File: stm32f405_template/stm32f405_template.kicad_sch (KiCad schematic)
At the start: 55 parts, among them J1 USB_B, J2 Conn_01x08, J3 Conn_01x08, J4 Conn_01x02, J5 Conn_01x08, J6 Conn_01x08, J7 Conn_01x02, J8 Conn_01x02, Q1 2N3904, Q2 2N3904, SW1 SW_RESET, U1 STM32F405RGTx, U2 MCP1700-3302E_TO92, Y1 14MHz, Y2 32.768 kHz

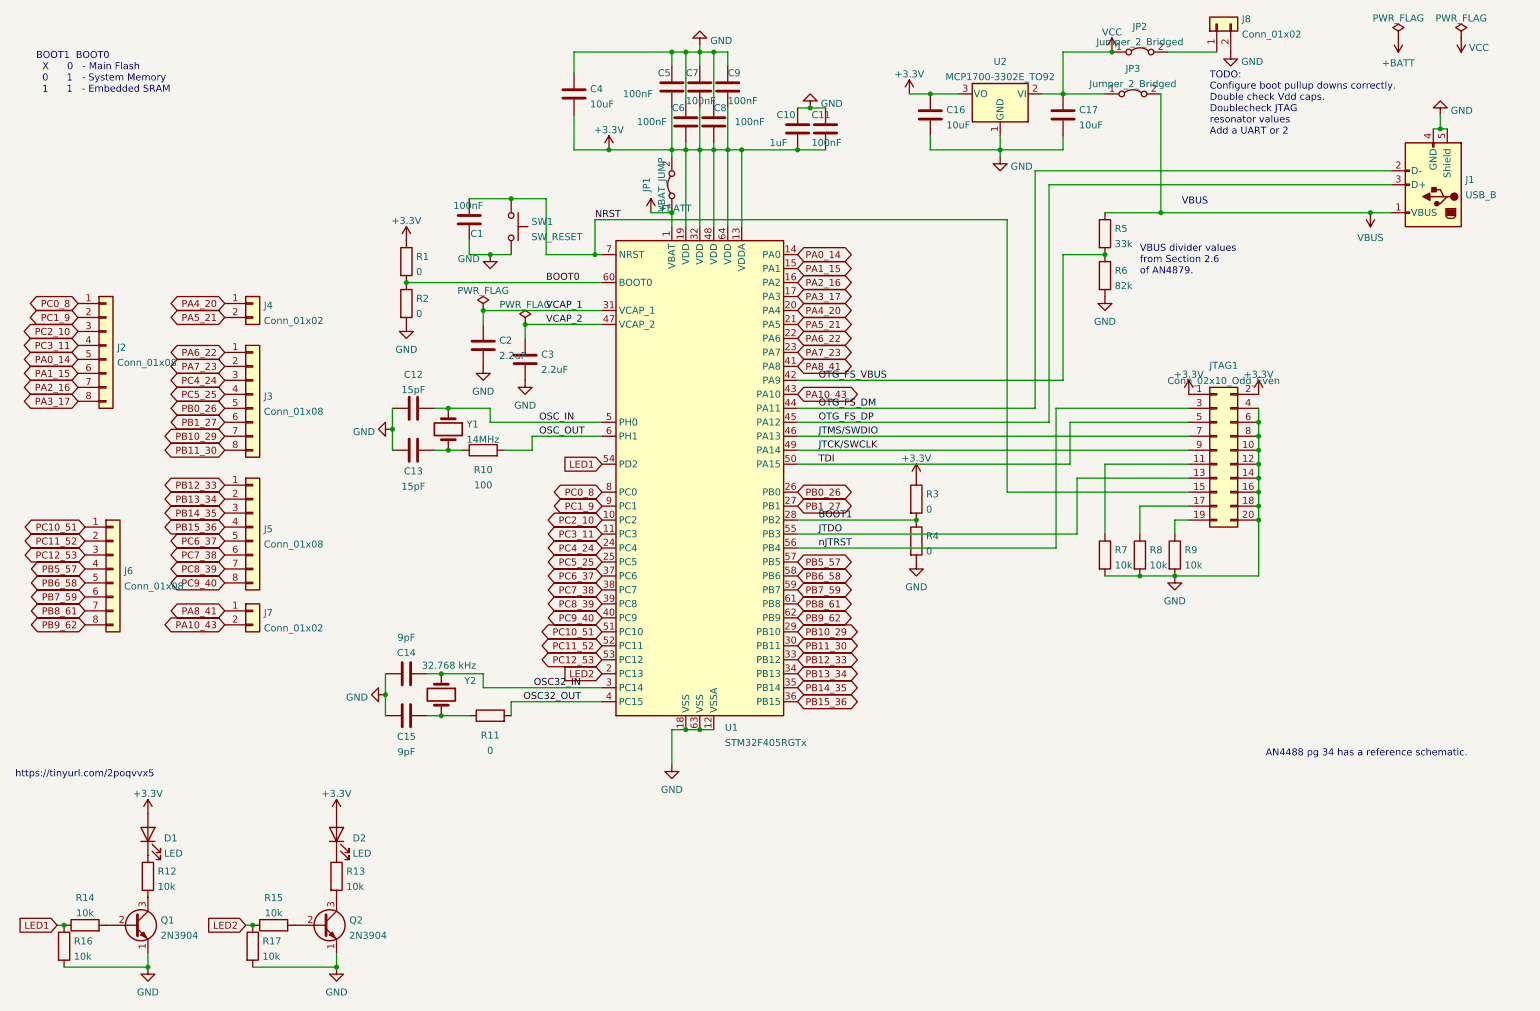
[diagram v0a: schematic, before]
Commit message: Geographic re-annotate and cleanup
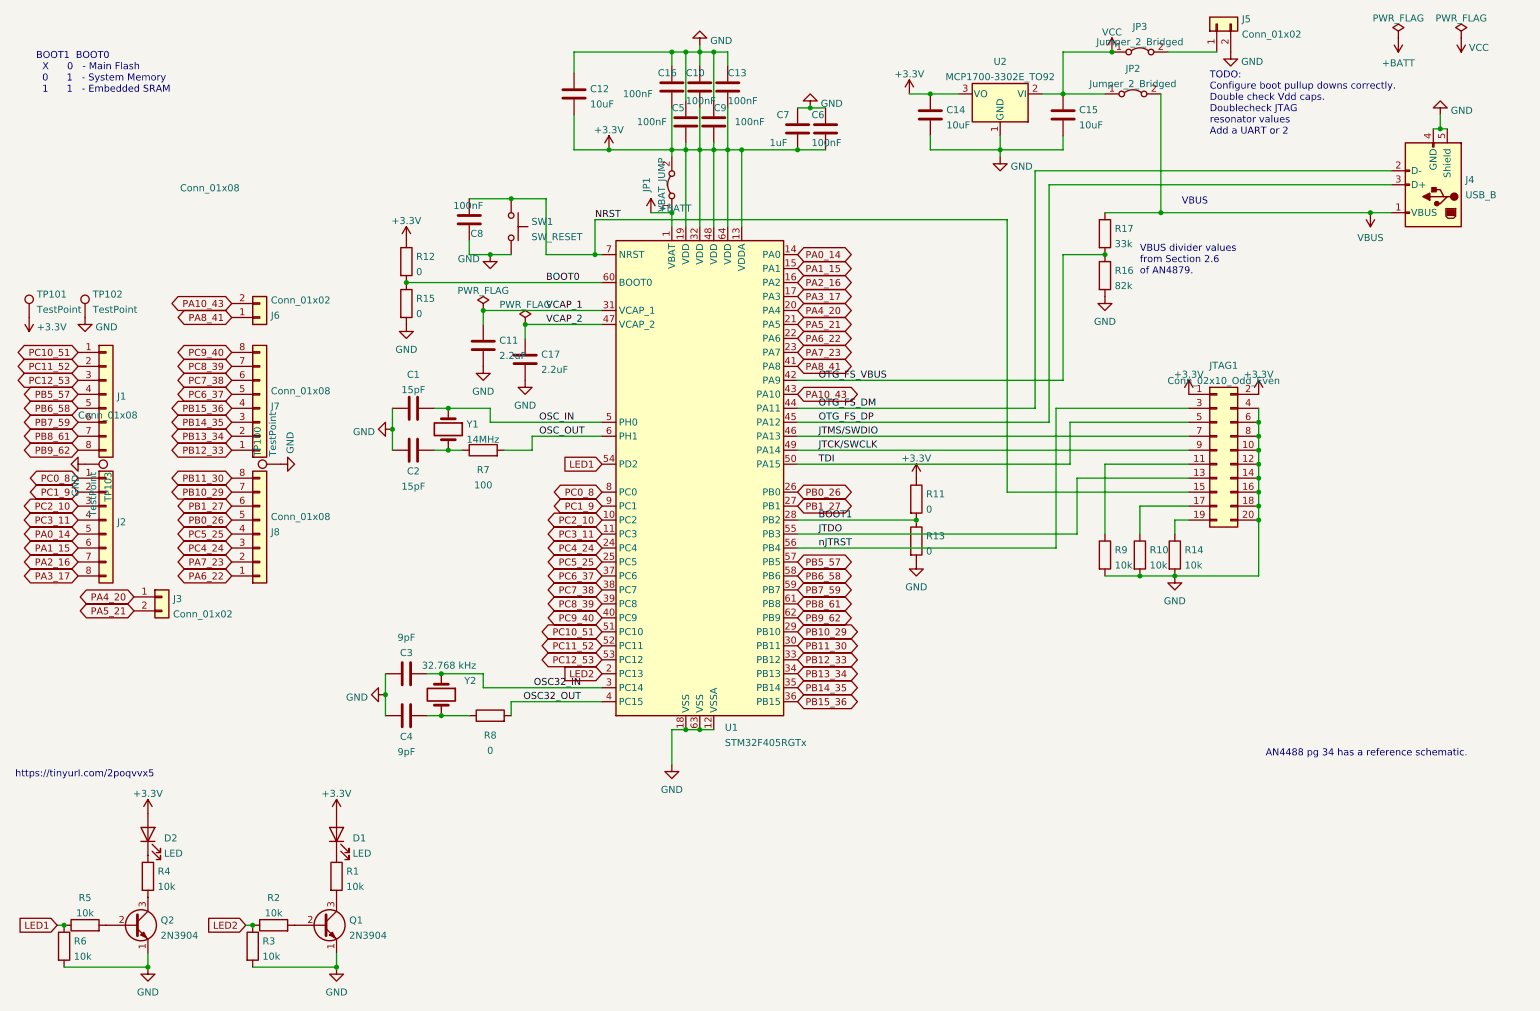
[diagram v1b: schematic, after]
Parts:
- added TP100, TP102, TP103: TestPoint, TestPoint:TestPoint_THTPad_1.5x1.5mm_Drill0.7mm, symbol Connector:TestPoint
- added TP101: TestPoint, TestPoint:TestPoint_THTPad_D1.5mm_Drill0.7mm, symbol Connector:TestPoint
- renumbered C12 to C1, C7 to C10, C2 to C11, C4 to C12, C9 to C13, C16 to C14, C17 to C15, C5 to C16, C3 to C17, C13 to C2, C14 to C3, C15 to C4, C6 to C5, C11 to C6, C10 to C7, C1 to C8, C8 to C9, D2 to D1, D1 to D2, J6 to J1, J4 to J3, J1 to J4, J8 to J5, J7 to J6, J5 to J7, J3 to J8, JP3 to JP2, JP2 to JP3, Q2 to Q1, Q1 to Q2, R13 to R1, R8 to R10, R3 to R11, R1 to R12, R4 to R13, R9 to R14, R2 to R15, R6 to R16, R5 to R17, R15 to R2, R17 to R3, R12 to R4, R14 to R5, R16 to R6, R10 to R7, R11 to R8, R7 to R9
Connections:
- net +3.3V: now also TP101.1
- net GND: now also TP100.1, TP102.1, TP103.1
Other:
- moved on the sheet: J1, J2, J3, J6, J7, J8

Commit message: Tidied silkscreen and some routing cleanup
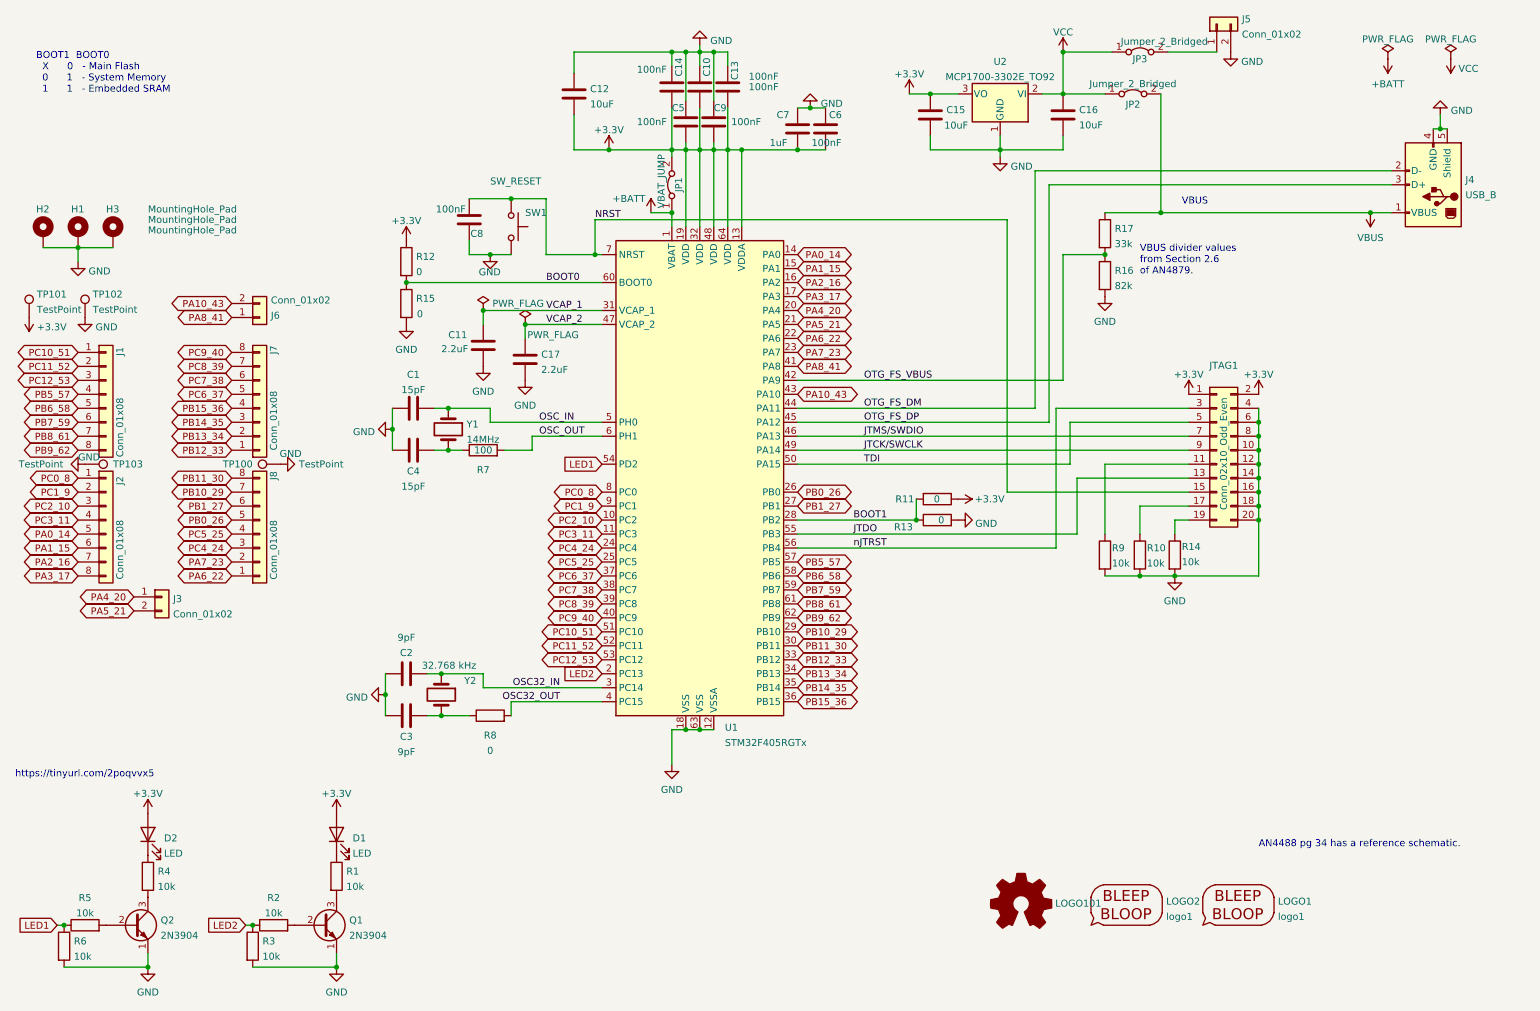
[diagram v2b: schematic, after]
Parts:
- added H1, H2, H3: MountingHole_Pad, MountingHole:MountingHole_3.2mm_M3_DIN965_Pad_TopBottom, symbol Mechanical:MountingHole_Pad
- added LOGO1: logo1, Symbol:OSHW-Symbol_6.7x6mm_SilkScreen, symbol My Stuff:logo1
- added LOGO101: Logo_Open_Hardware_Small, Symbol:OSHW-Symbol_6.7x6mm_SilkScreen, symbol My Stuff:Logo_Open_Hardware_Small
- added LOGO2: logo1, My Stuff:Logo1, symbol My Stuff:logo1
- C14: renamed from C16; footprint Capacitor_SMD:C_1206_3216Metric_Pad1.33x1.80mm_HandSolder -> Capacitor_THT:C_Disc_D5.0mm_W2.5mm_P5.00mm
- C16: renamed from C15; footprint Capacitor_THT:C_Disc_D5.0mm_W2.5mm_P5.00mm -> Capacitor_SMD:C_1206_3216Metric_Pad1.33x1.80mm_HandSolder
- renumbered C14 to C15, C3 to C2, C4 to C3, C2 to C4
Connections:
- net GND: now also H1.1, H2.1, H3.1
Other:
- note removed: "TODO: Configure boot pullup downs correctly. Double check Vdd caps. Doublecheck JTAG resonator values Add a UART or 2"
- company: (none) -> RobotDialogs
- title: (none) -> STM32 Breakout Board
- moved on the sheet: R11, R13

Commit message: v1 schematic pdf with some assembly updates and notes
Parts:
- C1, C4: value 15pF -> 10pF
- C14: footprint Capacitor_THT:C_Disc_D5.0mm_W2.5mm_P5.00mm -> Capacitor_SMD:C_1206_3216Metric_Pad1.33x1.80mm_HandSolder
- C16: footprint Capacitor_SMD:C_1206_3216Metric_Pad1.33x1.80mm_HandSolder -> Capacitor_THT:C_Disc_D5.0mm_W2.5mm_P5.00mm
- C2, C3: value 9pF -> 15pF
- R1, R4: value 10k -> 250
- R7: value 100 -> 40max
- R8: value 0 -> 50k max
- Y1: value 14MHz -> 16MHz
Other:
- note added: "CL = 6.0pF to 12.5pF CL = (CL1=Cl2)/2 CL1=CL2= 15pF/2=7.5pF"
- note added: "CL=5~50pF -> CL=(CL1=CL2)/2 -> 10pF/2=5pF SR = 40 Ohm Max"
